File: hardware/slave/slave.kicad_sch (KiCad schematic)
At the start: 37 parts, among them U1 ATtiny1604-SS

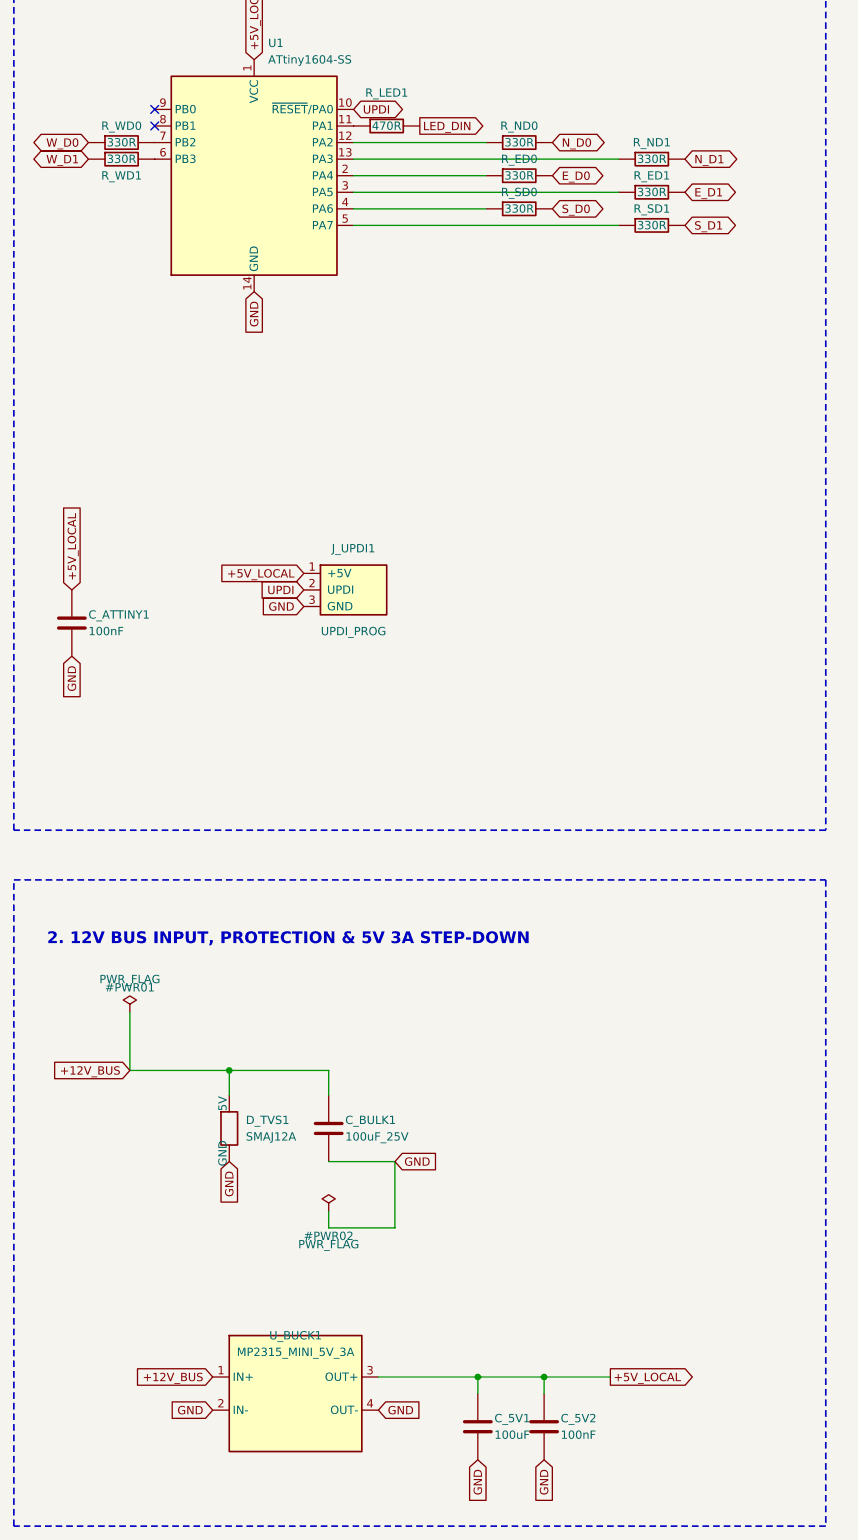
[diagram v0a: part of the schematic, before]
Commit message: feat(hardware): reorganize project structure, add master PCB, and update component libraries
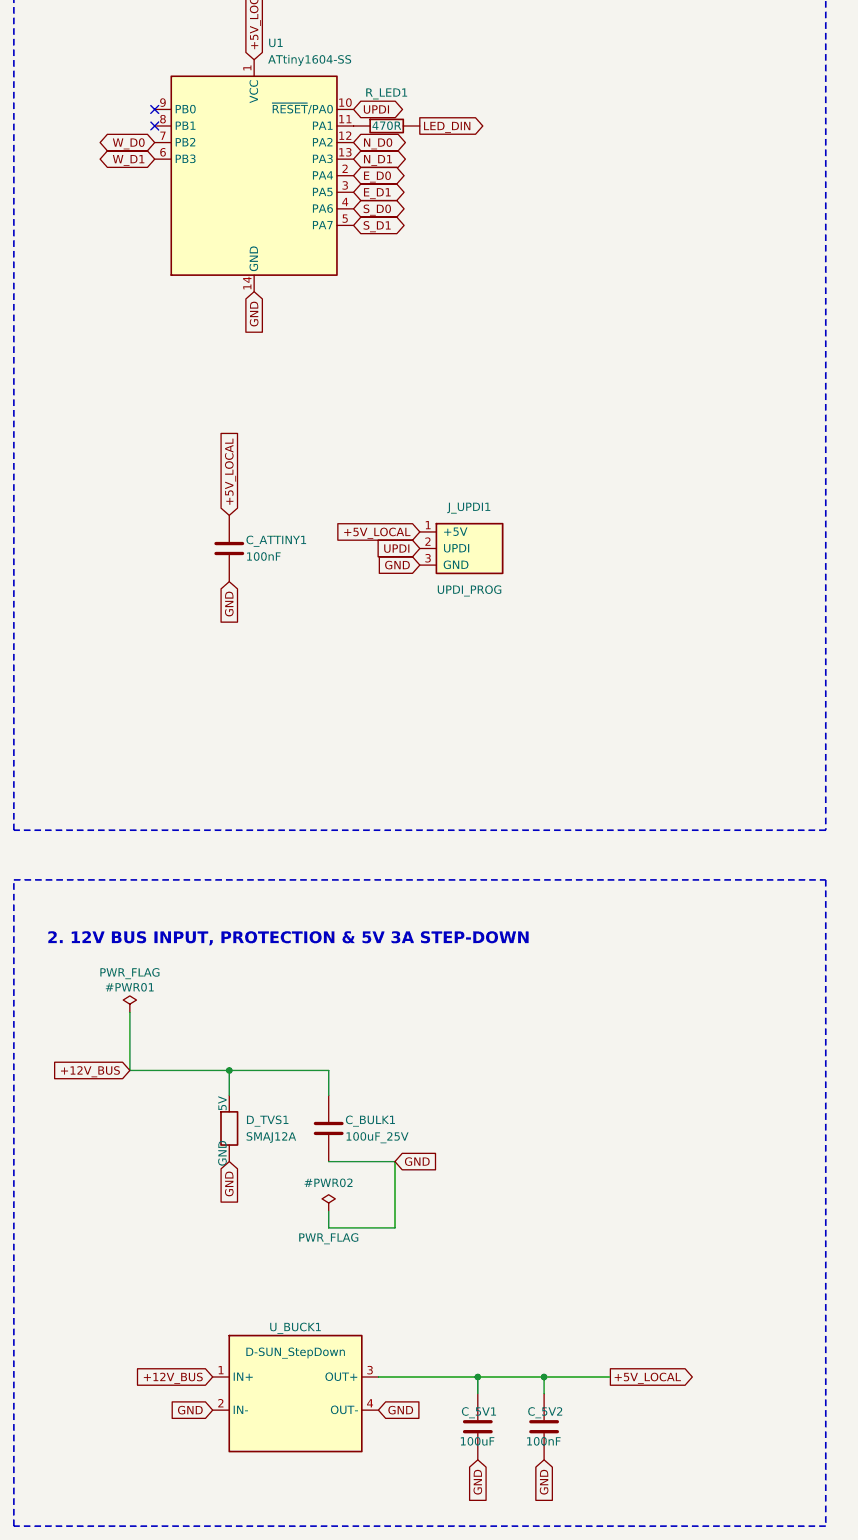
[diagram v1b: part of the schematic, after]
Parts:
- removed R_ED0, R_ED1, R_ND0, R_ND1, R_SD0, R_SD1, R_WD0, R_WD1: 330R, Resistor_SMD:R_0603_1608Metric, symbol board_game:Series_Resistor
- J_UPDI1: footprint Connector_PinHeader_2.54mm:PinHeader_1x03_P2.54mm_Vertical -> pin-header-1x03-smd:pin-header-1x03-smd
- U_BUCK1: value MP2315_MINI_5V_3A -> D-SUN_StepDown; footprint Module:MP2315_Mini_StepDown -> d-sun-stepdown:d-sun-stepdown; symbol board_game:MP2315_StepDown -> d-sun-stepdown:d-sun-stepdown
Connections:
- net E_D0: now also U1.2 (PA4)
- net E_D1: now also U1.3 (PA5)
- net N_D0: now also U1.12 (PA2)
- net N_D1: now also U1.13 (PA3)
- net S_D0: now also U1.4 (PA6)
- net S_D1: now also U1.5 (PA7)
- net W_D0: now also U1.7 (PB2)
- net W_D1: now also U1.6 (PB3)
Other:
- moved on the sheet: C_ATTINY1, J_UPDI1

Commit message: feat: add hardware firmware suite and update KiCad master/slave PCB designs
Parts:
- removed C_5V1: 100uF, Capacitor_SMD:C_1206_3216Metric, symbol board_game:Capacitor
- removed C_5V2: 100nF, Capacitor_SMD:C_0603_1608Metric, symbol board_game:Capacitor
- J_EAST1, J_NORTH1: footprint (none) -> magnetic-connector:fakemag6pin90degFemale
- J_SOUTH1, J_WEST1: footprint (none) -> magnetic-connector:fakemag6pin90degMale
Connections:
- net GND: now also MOD10.4 (GND_IN2), MOD11.4 (GND_IN2), MOD12.4 (GND_IN2), MOD14.4 (GND_IN2), MOD15.4 (GND_IN2), MOD16.4 (GND_IN2), MOD2.4 (GND_IN2), MOD3.4 (GND_IN2), MOD4.4 (GND_IN2), MOD6.4 (GND_IN2), MOD7.4 (GND_IN2), MOD8.4 (GND_IN2)
- net at MOD15.8 (GND_OUT2): no longer MOD16.4 (GND_IN2)
- net at MOD1.8 (GND_OUT2): no longer MOD2.4 (GND_IN2)
- net at MOD6.8 (GND_OUT2): no longer MOD7.4 (GND_IN2)
- net at MOD7.8 (GND_OUT2): no longer MOD8.4 (GND_IN2)
- net at MOD9.8 (GND_OUT2): no longer MOD10.4 (GND_IN2)
- net at MOD10.8 (GND_OUT2): no longer MOD11.4 (GND_IN2)
- net at MOD2.8 (GND_OUT2): no longer MOD3.4 (GND_IN2)
- net at MOD3.8 (GND_OUT2): no longer MOD4.4 (GND_IN2)
- net at MOD14.8 (GND_OUT2): no longer MOD15.4 (GND_IN2)
- net at MOD5.8 (GND_OUT2): no longer MOD6.4 (GND_IN2)
- net at MOD11.8 (GND_OUT2): no longer MOD12.4 (GND_IN2)
- net at MOD13.8 (GND_OUT2): no longer MOD14.4 (GND_IN2)
- no-connect marks 43 -> 55
